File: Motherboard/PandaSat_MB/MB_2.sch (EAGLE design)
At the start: 165 parts, among them J1 503182-1852, J14 M023.5MM_LOCK, J15 M023.5MM_LOCK, J16 M023.5MM_LOCK, J17 10118194-0001LF, J2 10118194-0001LF, J3 USBC, J4 BU-SMA-V, J5 BK-18650, K4 PE014006, Q1 IRLML2803, Q2 IRLML2803, Q3 IRLML2803, Q4 IRLML2803, Q5 MOSFET-PCHANNEL-SOIC8SOIC8, Q6 MOSFET-PCHANNEL-SOIC8SOIC8, Q7 MOSFET-PCHANNEL-SOIC8SOIC8, Q8 2N5088, U1 MAX706R, U10 DRV8848, U11 DRV8848, U12 MR25H40MDF, U2 LTC4121-4.2, U3 LSM9DS1, U4 MAX4372TEUK+T, U5 RFM23BP, U6 TPS54226PWPRPWP14_2P31X2P46-L, U7 ATSAMD51, U8 OKL-T3-W12

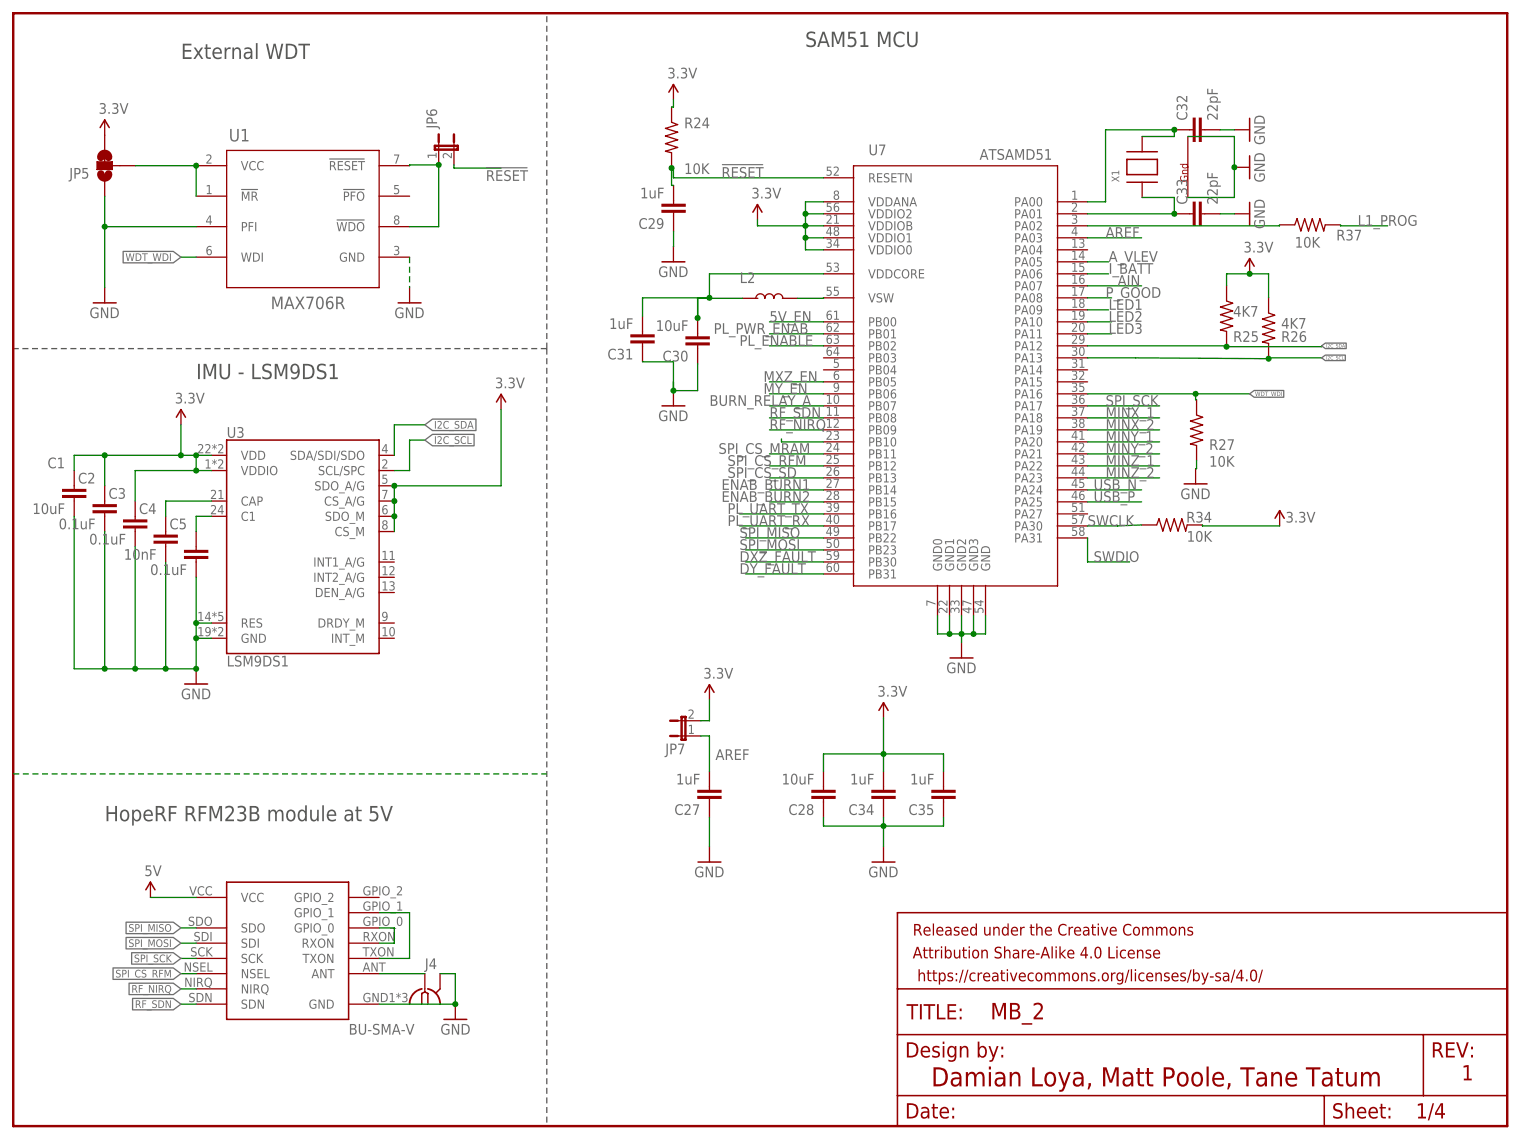
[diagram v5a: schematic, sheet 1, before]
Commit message: DRC error fixes, changed footprint for USB-C w/ milling layer
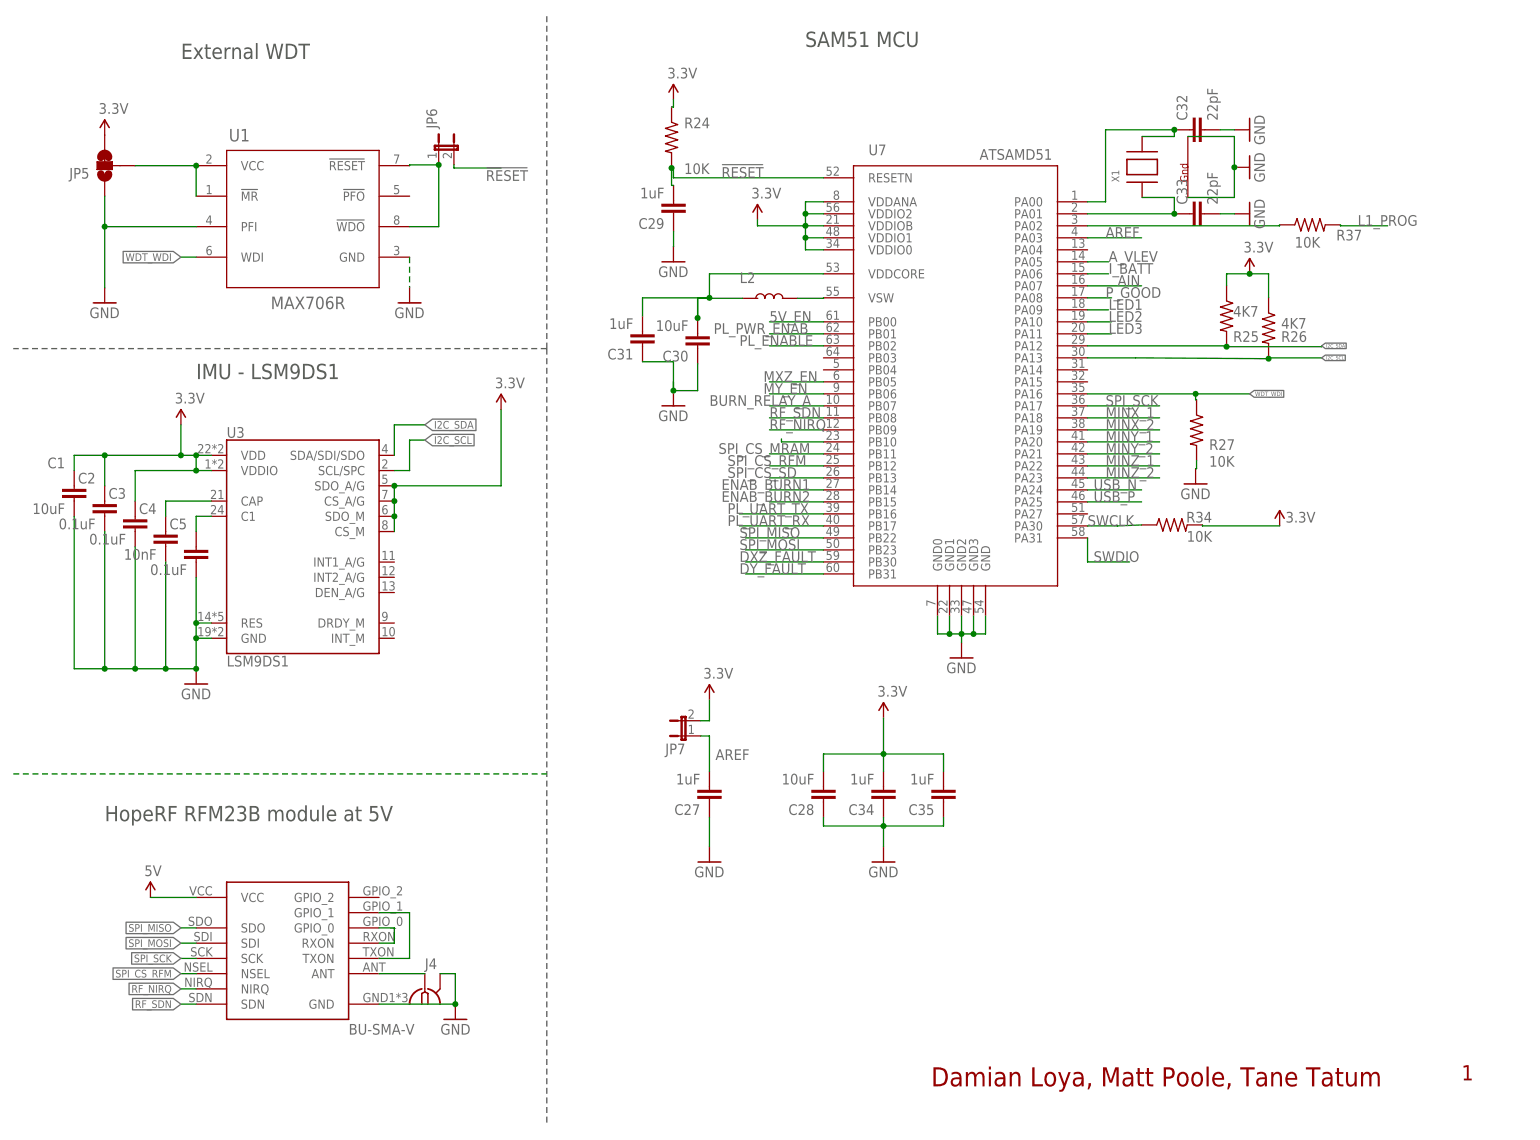
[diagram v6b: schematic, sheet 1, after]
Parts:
- removed FRAME1, FRAME2, FRAME3, FRAME4: FRAME-LETTER, SparkFun-Aesthetics:FRAME-LETTER
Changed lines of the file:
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@@
 <?xml version="1.0" encoding="utf-8"?>
 <!DOCTYPE eagle SYSTEM "eagle.dtd">
-<eagle version="9.3.0">
+<eagle version="9.2.2">
 <drawing>
 <settings>
@@
 <part name="LED5" library="adafruit" deviceset="LED" device="CHIP-LED0603"/>
 <part name="LED6" library="adafruit" deviceset="LED" device="CHIP-LED0603"/>
-<part name="FRAME1" library="SparkFun-Aesthetics" deviceset="FRAME-LETTER" device=""/>
-<part name="FRAME2" library="SparkFun-Aesthetics" deviceset="FRAME-LETTER" device=""/>
-<part name="FRAME3" library="SparkFun-Aesthetics" deviceset="FRAME-LETTER" device=""/>
-<part name="FRAME4" library="SparkFun-Aesthetics" deviceset="FRAME-LETTER" device=""/>
 </parts>
 <sheets>
@@
 <attribute name="NAME" x="121.03" y="140.46" size="1.778" layer="95"/>
 </instance>
-<instance part="FRAME1" gate="G$1" x="0" y="0" smashed="yes"/>
-<instance part="FRAME1" gate="G$2" x="147.32" y="0" smashed="yes">
-<attribute name="LAST_DATE_TIME" x="160.02" y="1.27" size="2.54" layer="94" font="vector"/>
-<attribute name="SHEET" x="233.68" y="1.27" size="2.54" layer="94" font="vector"/>
-<attribute name="DRAWING_NAME" x="162.814" y="17.78" size="2.7432" layer="94" font="vector"/>
-</instance>
 </instances>
 <busses>
@@
 <attribute name="VALUE" x="239.715" y="154.428" size="1.778" layer="96" rot="R90"/>
 </instance>
-<instance part="FRAME2" gate="G$1" x="0" y="0" smashed="yes"/>
-<instance part="FRAME2" gate="G$2" x="147.32" y="0" smashed="yes">
-<attribute name="LAST_DATE_TIME" x="160.02" y="1.27" size="2.54" layer="94" font="vector"/>
-<attribute name="SHEET" x="233.68" y="1.27" size="2.54" layer="94" font="vector"/>
-<attribute name="DRAWING_NAME" x="162.814" y="17.78" size="2.7432" layer="94" font="vector"/>
-</instance>
 </instances>
 <busses>
@@
 <attribute name="VALUE" x="29.43" y="114.08" size="1.778" layer="96" align="center-left"/>
 </instance>
-<instance part="FRAME3" gate="G$1" x="0" y="0" smashed="yes"/>
-<instance part="FRAME3" gate="G$2" x="147.32" y="0" smashed="yes">
-<attribute name="LAST_DATE_TIME" x="160.02" y="1.27" size="2.54" layer="94" font="vector"/>
-<attribute name="SHEET" x="233.68" y="1.27" size="2.54" layer="94" font="vector"/>
-<attribute name="DRAWING_NAME" x="162.814" y="17.78" size="2.7432" layer="94" font="vector"/>
-</instance>
 </instances>
 <busses>
@@
 <attribute name="VALUE" x="181.86" y="127.84" size="1.778" layer="96"/>
 </instance>
-<instance part="FRAME4" gate="G$1" x="0" y="0" smashed="yes"/>
-<instance part="FRAME4" gate="G$2" x="147.32" y="0" smashed="yes">
-<attribute name="LAST_DATE_TIME" x="160.02" y="1.27" size="2.54" layer="94" font="vector"/>
-<attribute name="SHEET" x="233.68" y="1.27" size="2.54" layer="94" font="vector"/>
-<attribute name="DRAWING_NAME" x="162.814" y="17.78" size="2.7432" layer="94" font="vector"/>
-</instance>
 </instances>

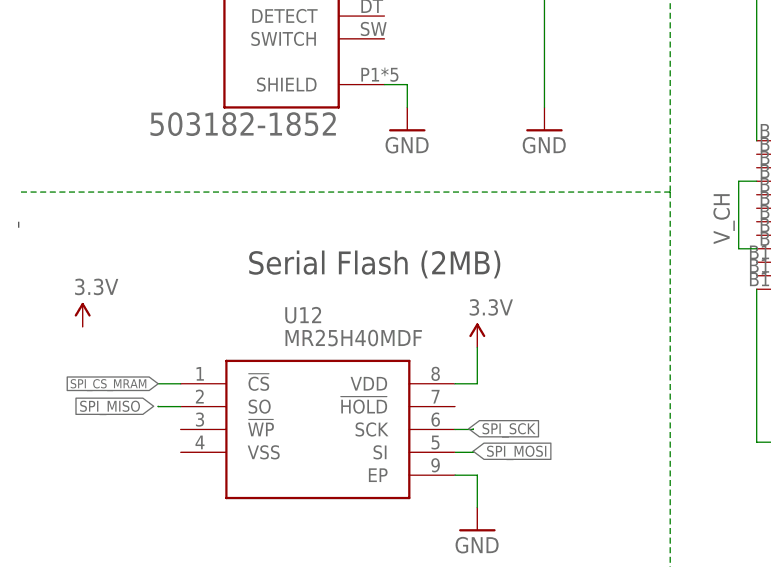
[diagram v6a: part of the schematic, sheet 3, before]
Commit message: Changed connector config and DRC stuff for Y panel
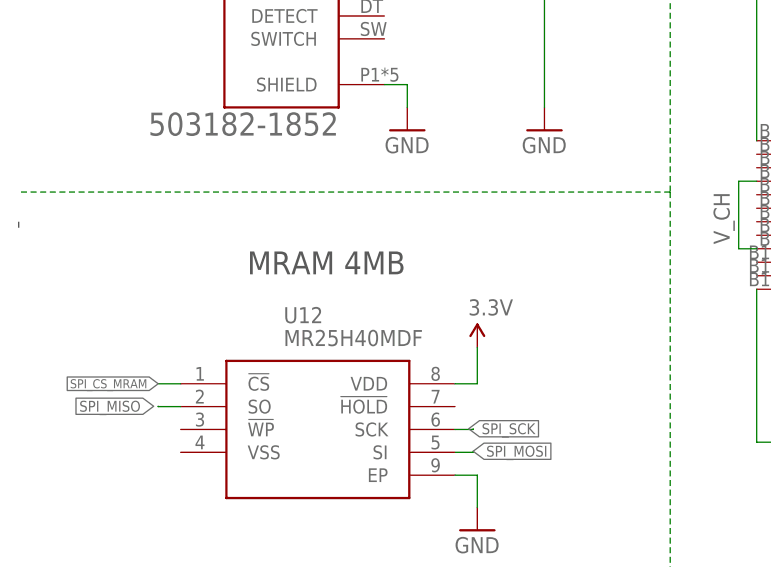
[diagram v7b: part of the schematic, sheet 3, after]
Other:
- note added: "MRAM 4MB"
- note removed: "Serial Flash (2MB)"
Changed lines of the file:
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@@
 <part name="R34" library="resistor" library_urn="urn:adsk.eagle:library:348" deviceset="R-US_" device="R0603" package3d_urn="urn:adsk.eagle:package:26057/1" value="10K"/>
 <part name="SUPPLY18" library="SparkFun-Aesthetics" deviceset="3.3V" device=""/>
-<part name="SUPPLY19" library="SparkFun-Aesthetics" deviceset="3.3V" device=""/>
 <part name="C36" library="SparkFun-Capacitors" deviceset="CAP" device="0603-CAP" value="2.2uF">
 <attribute name="VOLTAGE" value="6.3V"/>
@@
 <text x="27.94" y="180.34" size="2.54" layer="97">MicroSD Card</text>
 <wire x1="0" y1="127" x2="0" y2="126.238" width="0.1524" layer="97" style="longdash"/>
-<text x="25.4" y="123.698" size="2.54" layer="97" font="vector" align="top-left">Serial Flash (2MB)</text>
+<text x="25.4" y="123.698" size="2.54" layer="97" font="vector" align="top-left">MRAM 4MB</text>
 <text x="185.166" y="119.634" size="1.778" layer="97">Footswitch Connections</text>
 <text x="154.686" y="157.734" size="1.778" layer="97">Battery Terminals</text>
@@
 <attribute name="VALUE" x="136.652" y="143.51" size="1.778" layer="96" rot="R180"/>
 </instance>
-<instance part="SUPPLY19" gate="G$1" x="7.112" y="115.316" smashed="yes">
-<attribute name="VALUE" x="6.096" y="118.872" size="1.778" layer="96"/>
-</instance>
 <instance part="SUPPLY26" gate="G$1" x="20.574" y="69.088" smashed="yes">
